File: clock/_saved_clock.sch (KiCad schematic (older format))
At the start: 76 parts, among them J1 FTDI, J2 USB, J3 TP, SW1 SW_SPST, SW2 SW_SPST, SW3 SW_SPST, SW4 SW_SPST, SW5 SW_SPST, U1 iv12, U10 PCA9685PW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

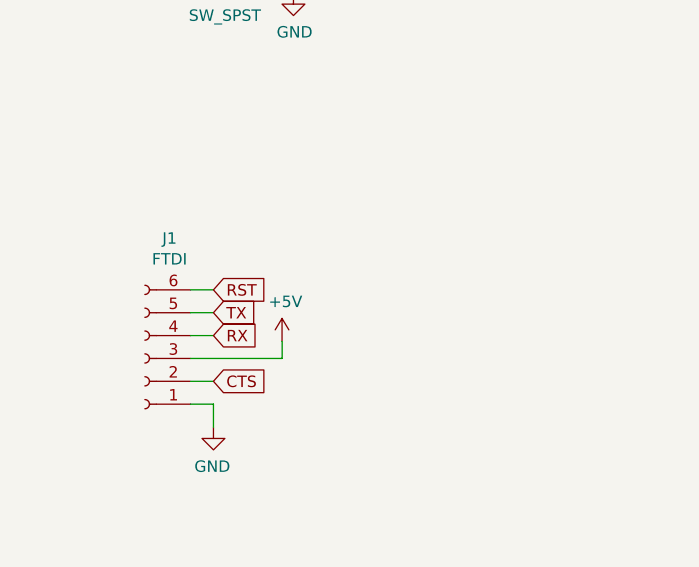
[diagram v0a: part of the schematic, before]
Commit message: Added capacitor to reset line
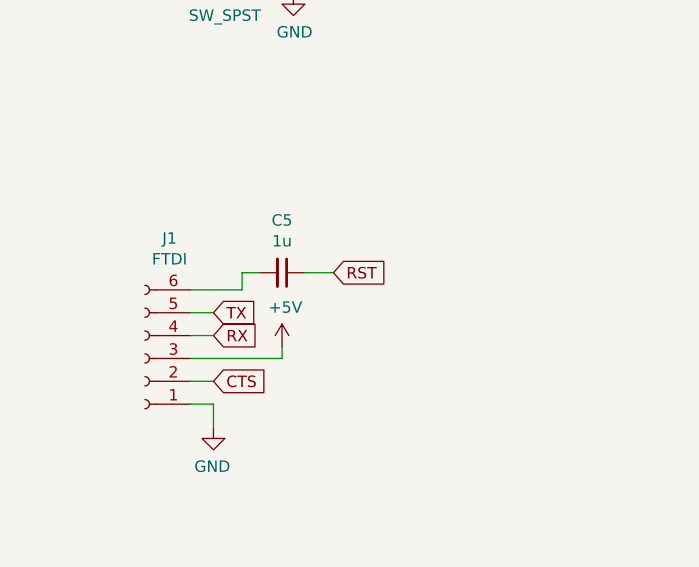
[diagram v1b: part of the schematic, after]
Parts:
- added C5: 1u, Capacitor_SMD:C_0603_1608Metric_Pad1.05x0.95mm_HandSolder, symbol Device:C_Small
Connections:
- net RST: now also C5.1; no longer J1.6 (Pin_6)
- new net: C5.2, J1.6 (Pin_6)
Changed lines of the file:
@@
 Wire Wire Line
 	1750 4200 1650 4200
-Text GLabel 1750 4100 2    50   Input ~ 0
+Text GLabel 2275 4025 2    50   Input ~ 0
 RST
-Wire Wire Line
-	1750 4100 1650 4100
 Text GLabel 6250 4750 2    50   Input ~ 0
 RX
@@
 L power:+5V #PWR0147
 U 1 1 5CA39077
-P 2050 4325
-F 0 "#PWR0147" H 2050 4175 50  0001 C CNN
-F 1 "+5V" H 2065 4498 50  0000 C CNN
-F 2 "" H 2050 4325 50  0001 C CNN
-F 3 "" H 2050 4325 50  0001 C CNN
-	1    2050 4325
+P 2050 4350
+F 0 "#PWR0147" H 2050 4200 50  0001 C CNN
+F 1 "+5V" H 2065 4523 50  0000 C CNN
+F 2 "" H 2050 4350 50  0001 C CNN
+F 3 "" H 2050 4350 50  0001 C CNN
+	1    2050 4350
 	1    0    0    -1
 $EndComp
@@
 	1650 4400 2050 4400
 Wire Wire Line
-	2050 4400 2050 4325
+	2050 4350 2050 4400
+$Comp
+L Device:C_Small C5
+U 1 1 5CA06683
+P 2050 4025
+F 0 "C5" V 1821 4025 50  0000 C CNN
+F 1 "1u" V 1912 4025 50  0000 C CNN
+F 2 "Capacitor_SMD:C_0603_1608Metric_Pad1.05x0.95mm_HandSolder" H 2050 4025 50  0001 C CNN
+F 3 "~" H 2050 4025 50  0001 C CNN
+	1    2050 4025
+	0    1    1    0
+$EndComp
+Wire Wire Line
+	2150 4025 2275 4025
+Wire Wire Line
+	1875 4100 1875 4025
+Wire Wire Line
+	1875 4025 1950 4025
+Wire Wire Line
+	1650 4100 1875 4100
 $EndSCHEMATC
